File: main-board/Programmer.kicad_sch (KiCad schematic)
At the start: 32 parts, among them U1 FT4232HL, U14 TS5A23159DGS, U28 TS5A23159DGS, U9 74AHCT1G08, Y1 Crystal_GND24

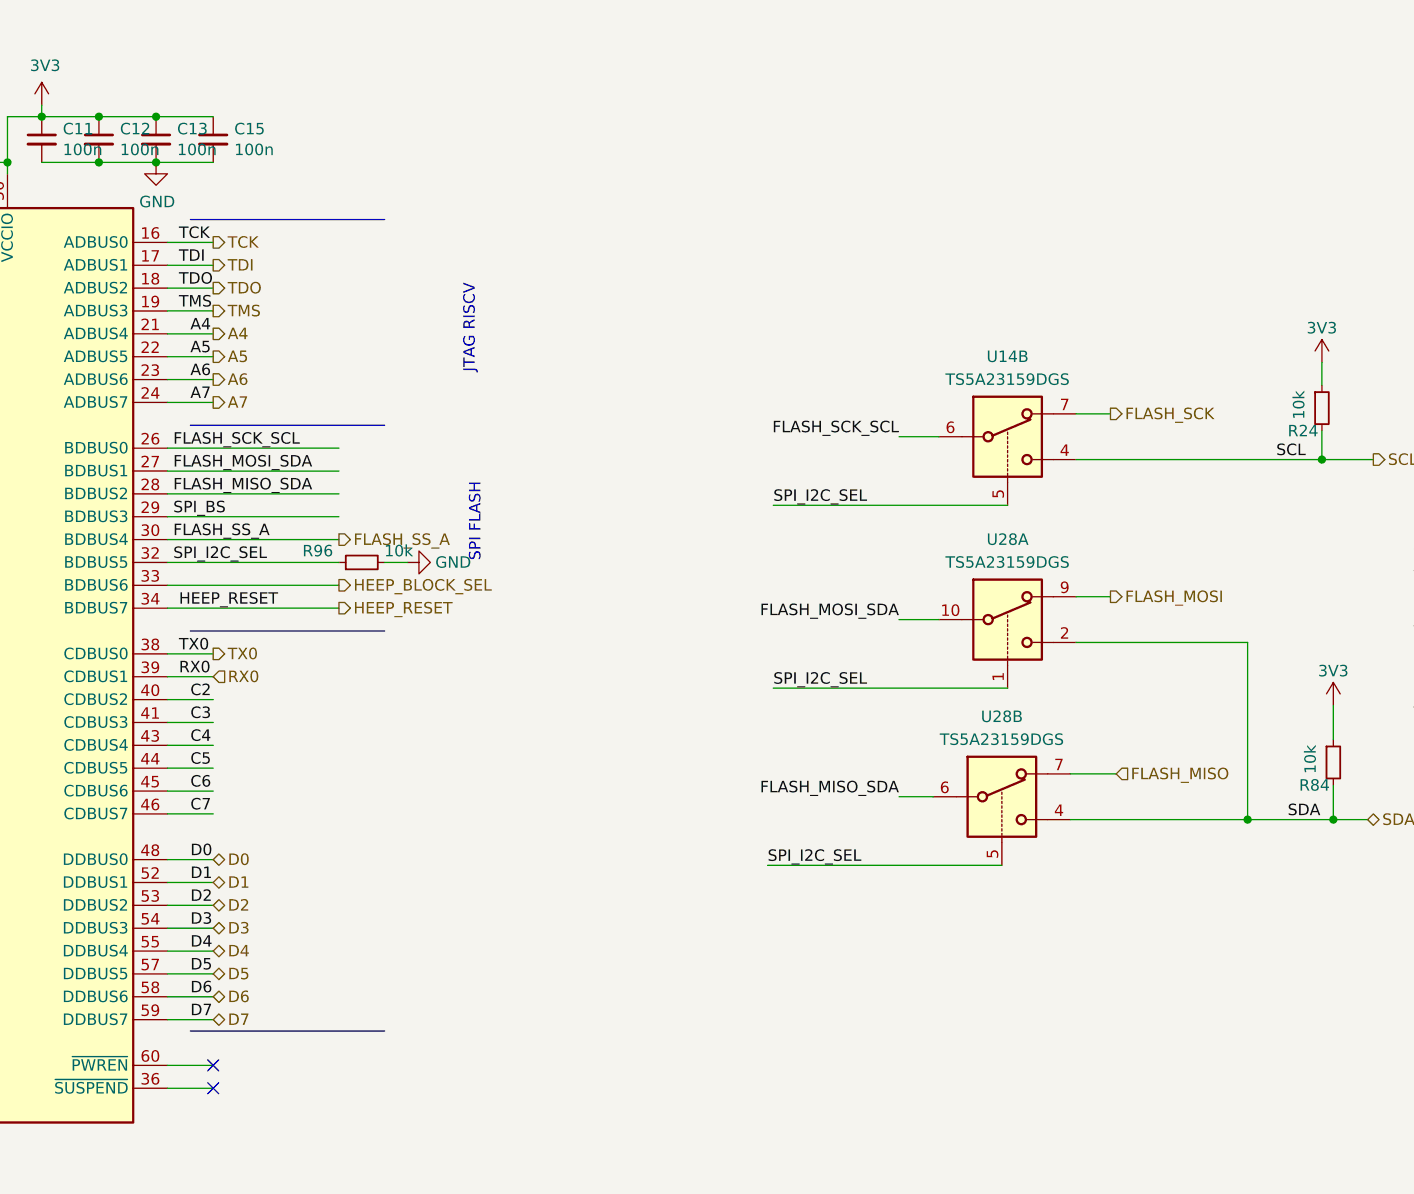
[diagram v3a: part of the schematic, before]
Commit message: WIP: added i2c expanders and re-structuring i2c distributino
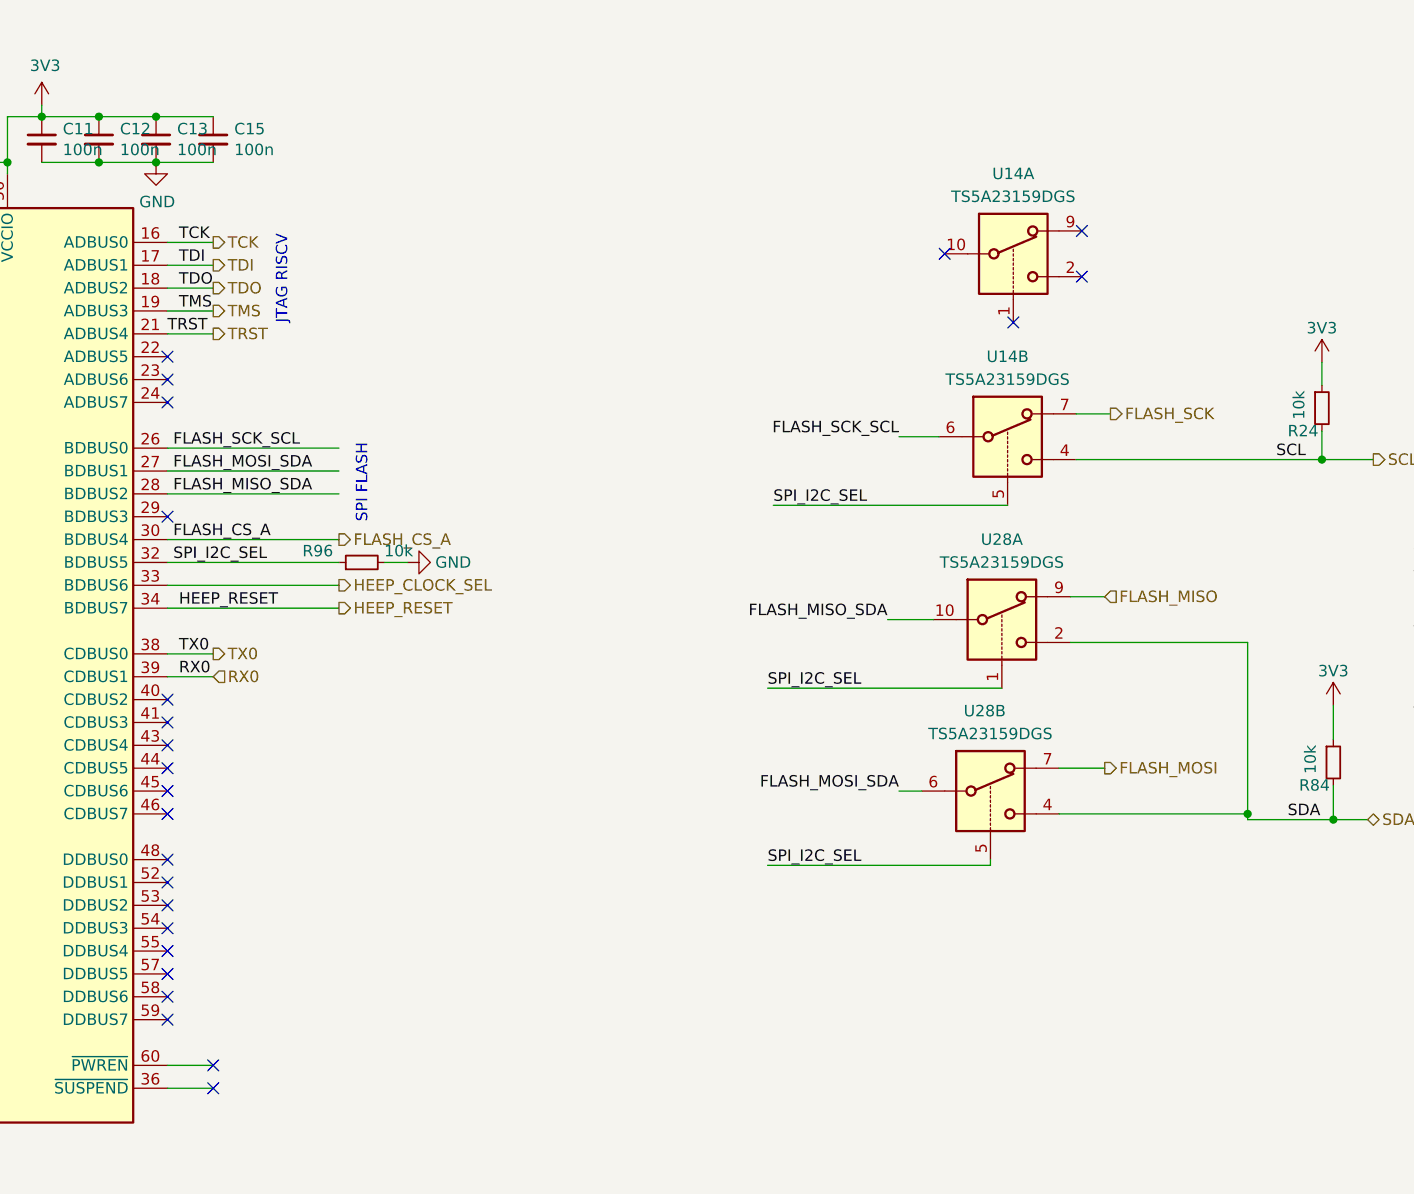
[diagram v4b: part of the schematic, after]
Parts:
- added unit 1 of U14
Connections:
- net FLASH_MISO: now also U28.9; no longer U28.7
- net FLASH_MISO_SDA: now also U28.10; no longer U28.6
- net FLASH_MOSI: now also U28.7; no longer U28.9
- net FLASH_MOSI_SDA: now also U28.6; no longer U28.10
- net A4 renamed TRST
- net A5: no longer names the net of U1.22 (ADBUS5)
- net A6: no longer names the net of U1.23 (ADBUS6)
- net A7: no longer names the net of U1.24 (ADBUS7)
- net C2: no longer names the net of U1.40 (CDBUS2)
- net C3: no longer names the net of U1.41 (CDBUS3)
- net C4: no longer names the net of U1.43 (CDBUS4)
- net C5: no longer names the net of U1.44 (CDBUS5)
- net C6: no longer names the net of U1.45 (CDBUS6)
- net C7: no longer names the net of U1.46 (CDBUS7)
- net D0: no longer names the net of U1.48 (DDBUS0)
- net D1: no longer names the net of U1.52 (DDBUS1)
- net D2: no longer names the net of U1.53 (DDBUS2)
- net D3: no longer names the net of U1.54 (DDBUS3)
- net D4: no longer names the net of U1.55 (DDBUS4)
- net D5: no longer names the net of U1.57 (DDBUS5)
- net D6: no longer names the net of U1.58 (DDBUS6)
- net D7: no longer names the net of U1.59 (DDBUS7)
- net FLASH_SS_A renamed FLASH_CS_A
- net HEEP_BLOCK_SEL renamed HEEP_CLOCK_SEL
- net SPI_BS: no longer names the net of U1.29 (BDBUS3)
- no-connect marks 2 -> 24
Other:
- moved on the sheet: U28A, U28B

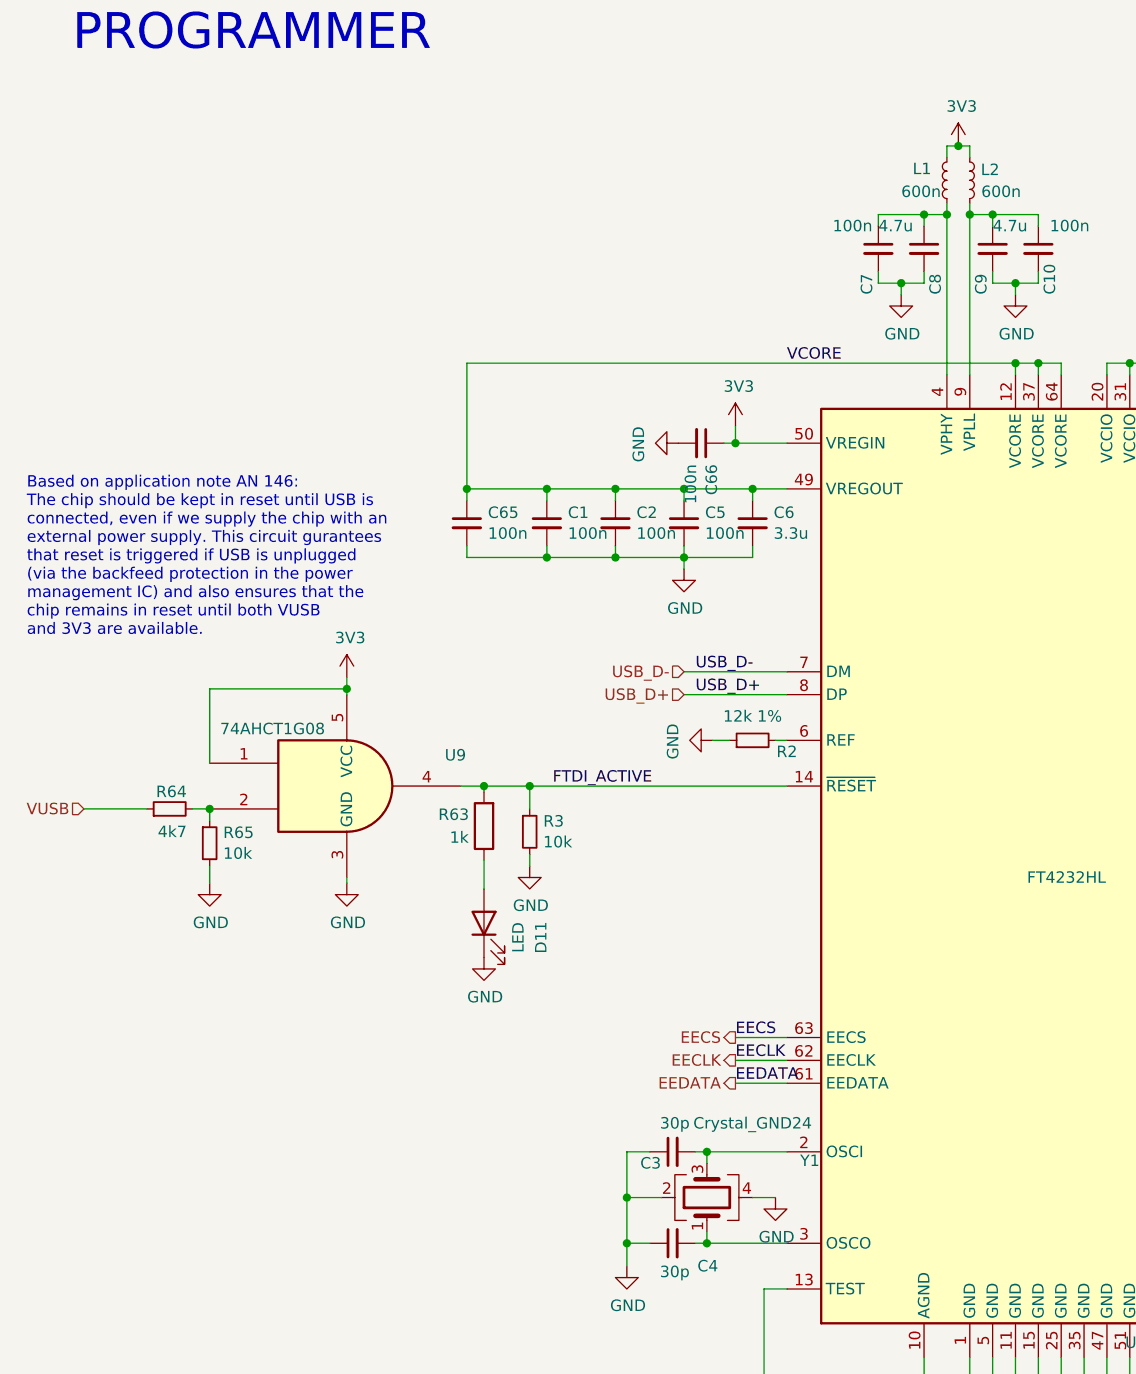
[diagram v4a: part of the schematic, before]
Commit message: rework main PCB: added USB-C, new connector symbol & footprints
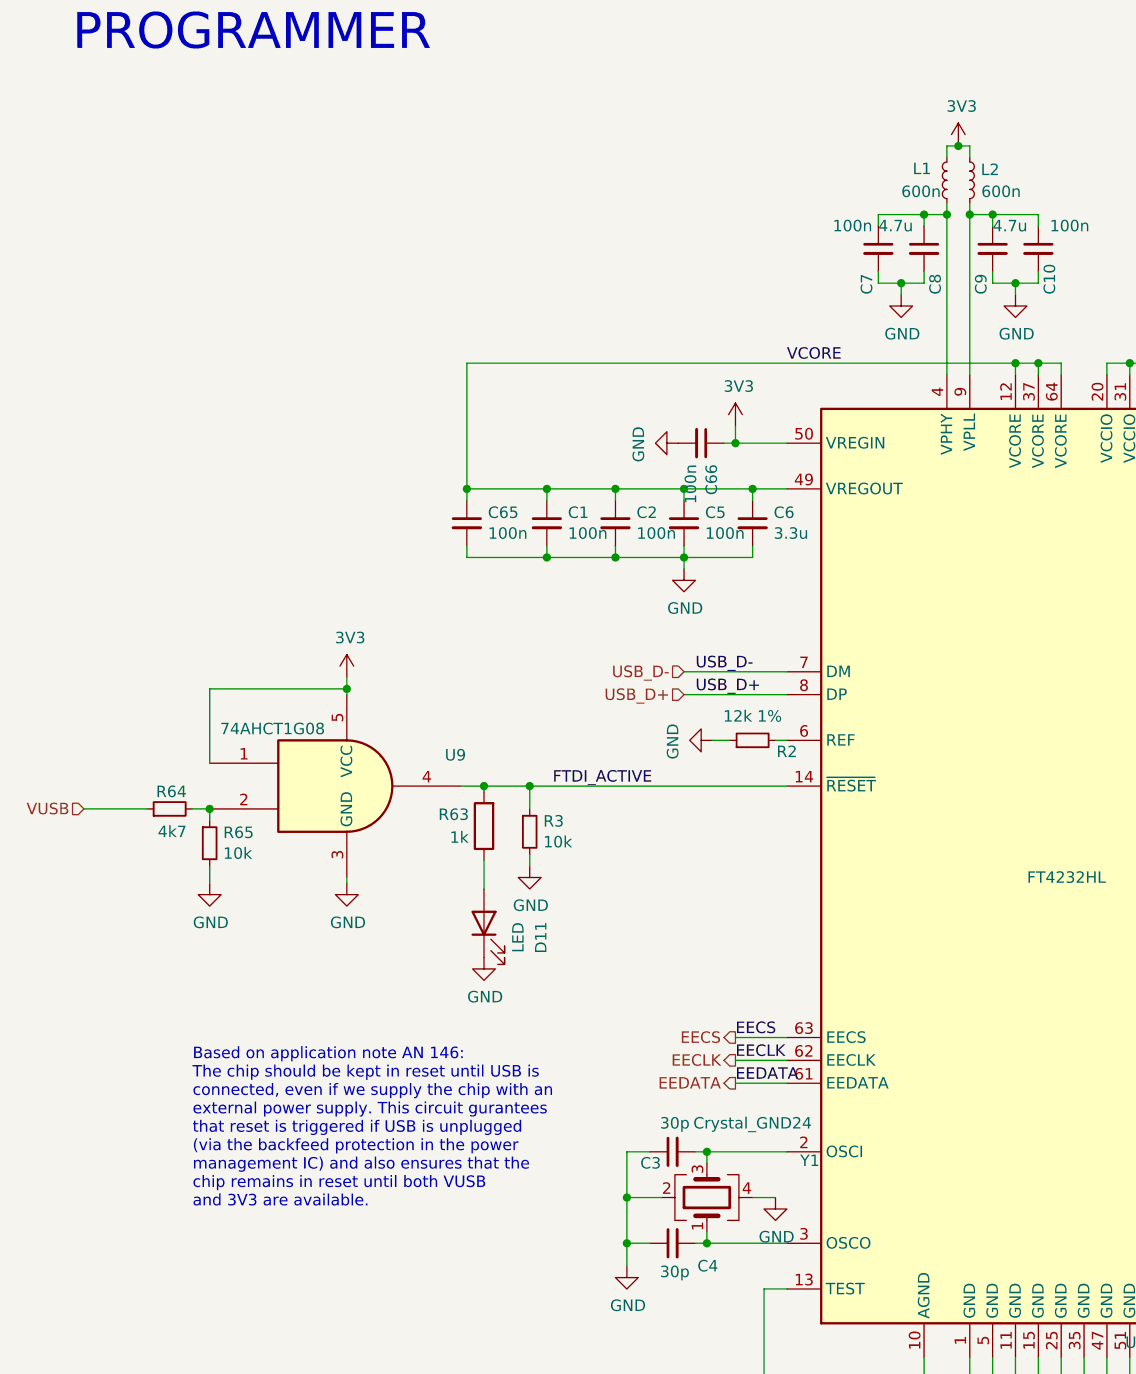
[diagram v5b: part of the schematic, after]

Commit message: PCB update
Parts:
- added C45, C50: 100nF, Capacitor_SMD:C_0603_1608Metric, symbol Device:C_Small
- added unit 3 of U14
- added unit 3 of U28
- C1, C10, C11, C12, C13, C15, C2, C5, C65, C66, C7: value 100n -> 100nF
- C3, C4: value 30p -> 30pF; LCSC (none) -> C1658
- C6: value 3.3u -> 3.3uF
- C8, C9: value 4.7u -> 4.7uF
- L1, L2: value 600n -> 600nH
- R2: LCSC (none) -> C22790
- R64: value 4k7 -> 4.7k; LCSC (none) -> C99782
- U14, U28: LCSC (none) -> C42751
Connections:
- net 3V3: now also C45.1, C50.1, U14.8 (VCC), U28.8 (VCC)
- net GND: now also C45.2, C50.2, U14.3 (GND), U28.3 (GND)
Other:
- moved on the sheet: R24, R84, U14B, U28A

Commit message: production files
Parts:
- L1, L2: footprint Inductor_SMD:L_0805_2012Metric -> Inductor_SMD:L_0603_1608Metric
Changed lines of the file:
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@@
 			)
 		)
-		(property "Footprint" "Inductor_SMD:L_0805_2012Metric"
+		(property "Footprint" "Inductor_SMD:L_0603_1608Metric"
 			(at 147.32 135.89 0)
 			(effects
@@
 			)
 		)
-		(property "Footprint" "Inductor_SMD:L_0805_2012Metric"
+		(property "Footprint" "Inductor_SMD:L_0603_1608Metric"
 			(at 144.78 135.89 0)
 			(effects
